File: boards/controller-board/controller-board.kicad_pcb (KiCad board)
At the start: 2 copper layers, 130 x 115 mm, 172 parts, among them J1 Conn_01x02, J2 Conn_01x02, J3 Conn_01x02, J4 Conn_01x02, J5 Conn_01x03, J6 Conn_01x02, Q1 Goford_G11S_20V_11A, Q2 PMV45EN, SW1 EG1271, U1 CAT4201, U10 CAT4201, U11 CAT4201, U12 CAT4201, U13 CAT4201, U14 CAT4201, U15 CAT4201, U17 CAT4201, U18 CAT4201, U25 RPi_Pico, U3 LTC3624, U4 CAT4201, U5 CAT4201, U6 CAT4201, U7 MCP4728, U8 ADS1015IRUGR, U9 ADS1015IRUGR

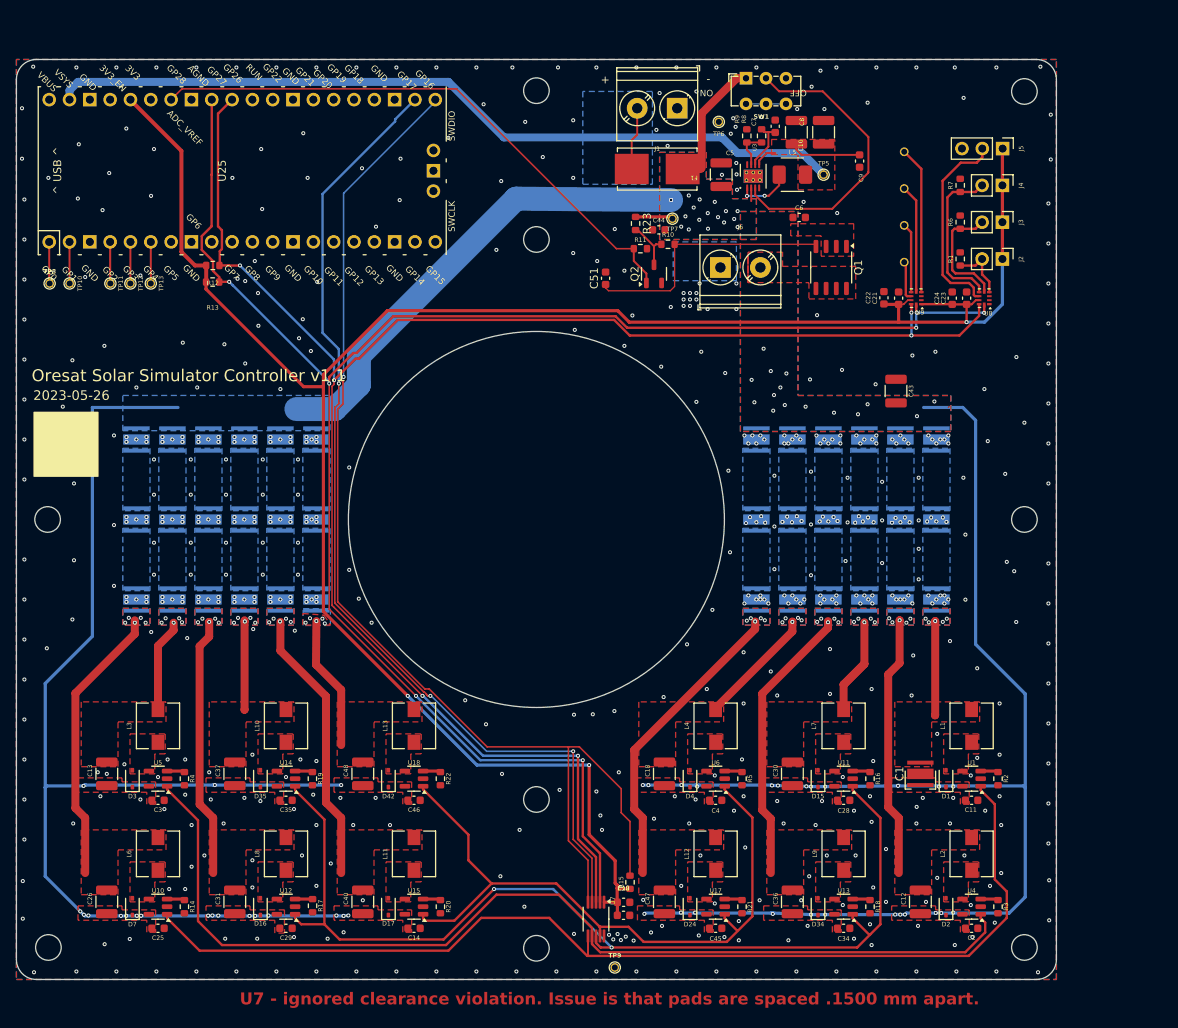
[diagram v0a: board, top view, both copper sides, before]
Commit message: added ground vias and changed ground pad filling on some components
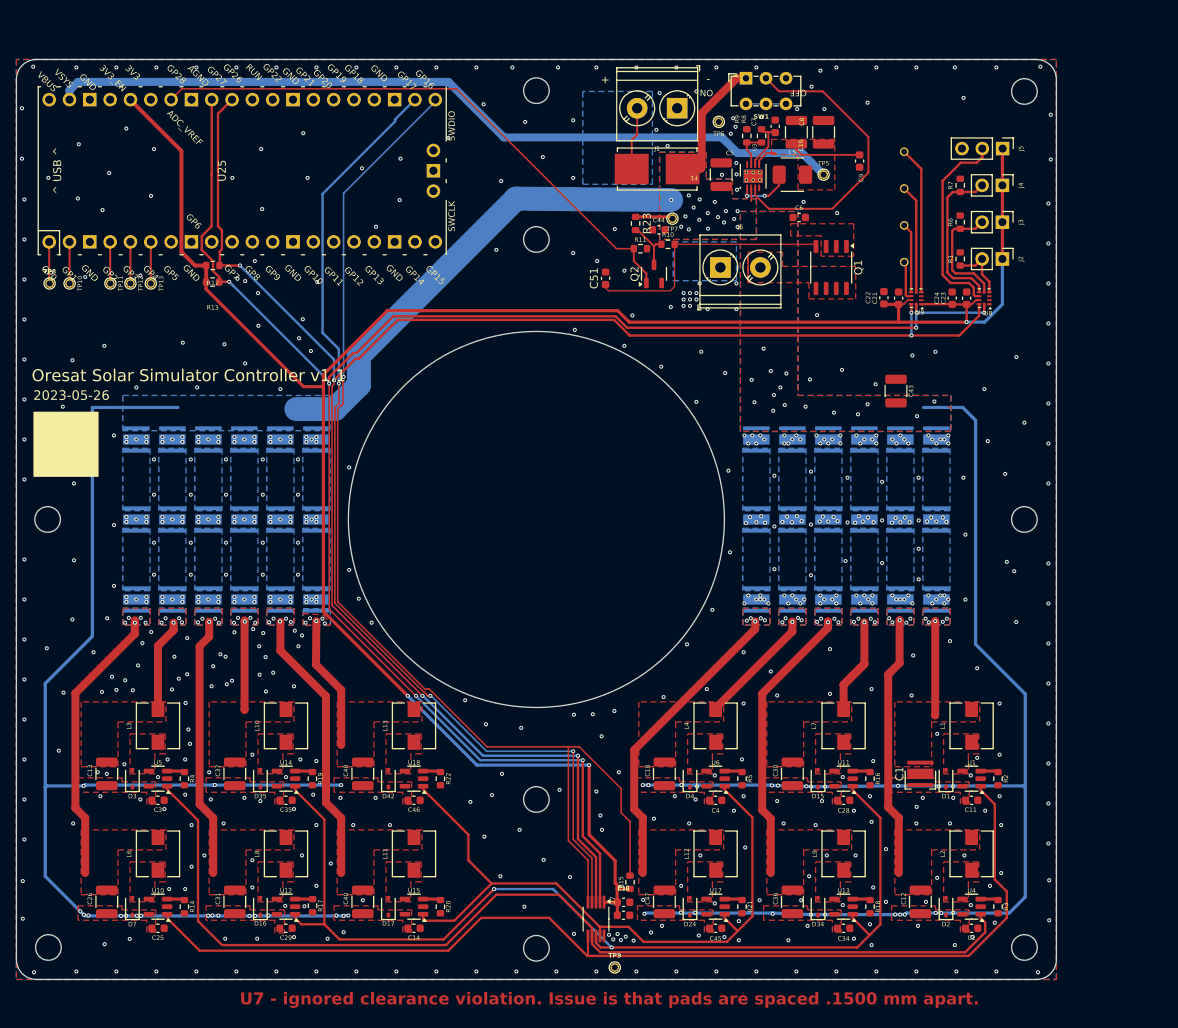
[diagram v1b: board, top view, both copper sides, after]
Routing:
- net VCC: vias 76 -> 75
- net GND: vias 591 -> 634

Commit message: added new design for LED driver portion of circuit with A6214
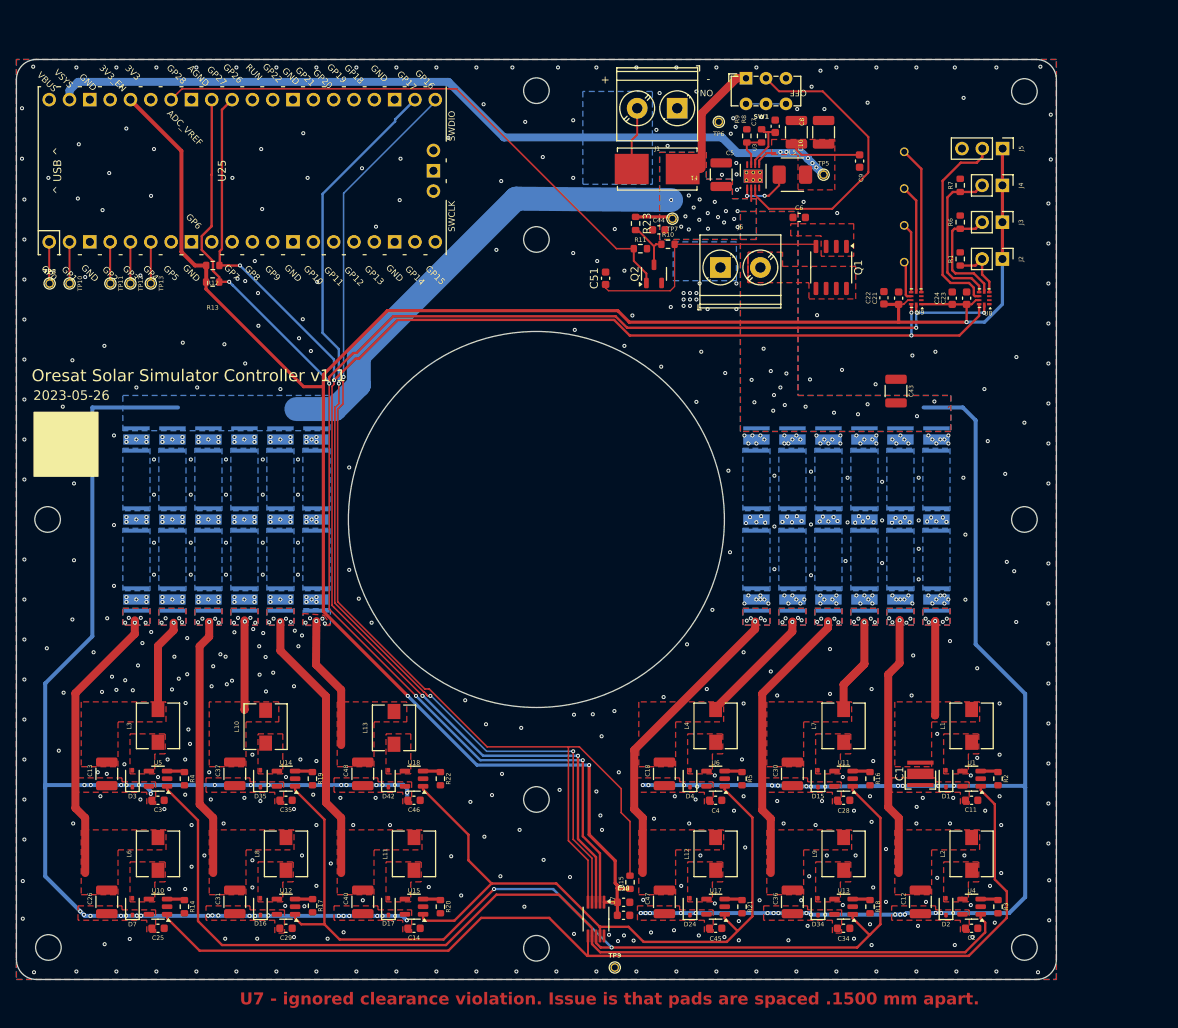
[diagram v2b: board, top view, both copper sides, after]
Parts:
- moved L10 2.55 mm to (111.2, 128.4)
- moved L13 2.51 mm to (127.2, 128.6)
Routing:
- net VCC: track 398.8 -> 417.2 mm, vias 75 -> 97
- net +5V: track 112.5 -> 111.9 mm, vias 0 -> 5
- net GND: vias 634 -> 635

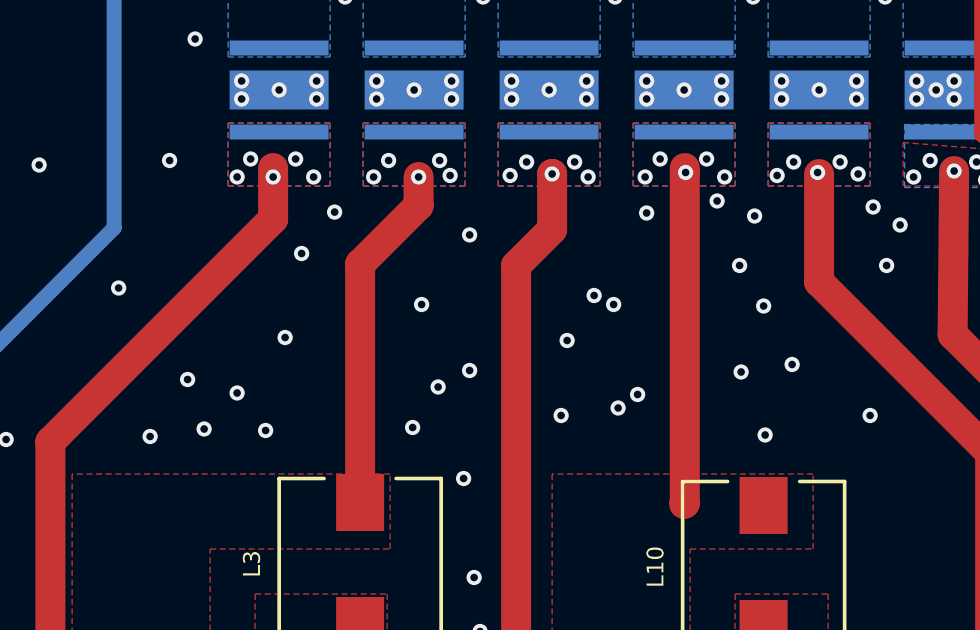
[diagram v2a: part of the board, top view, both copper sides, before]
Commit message: added project for test board for new LED driver
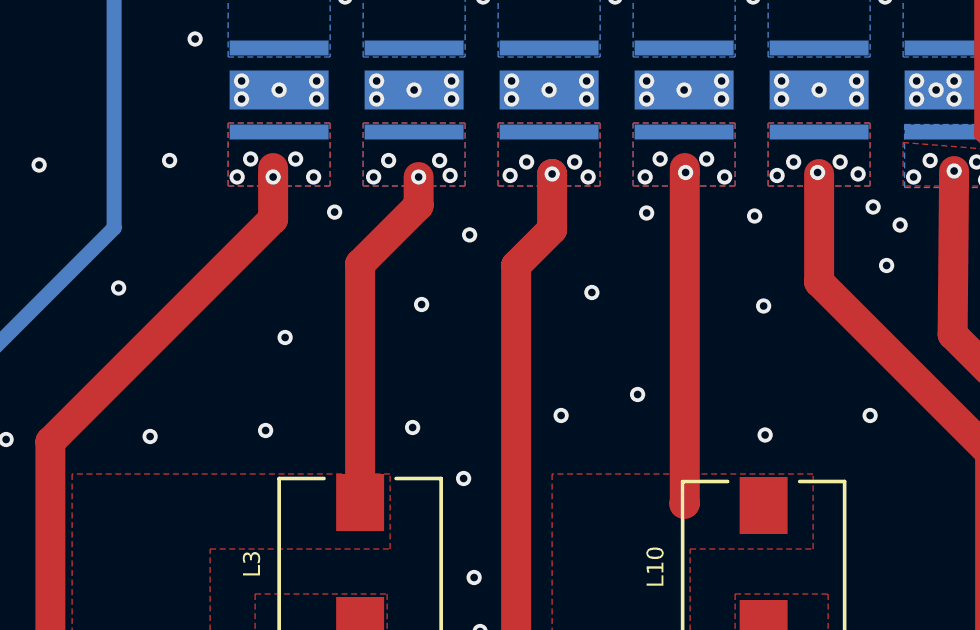
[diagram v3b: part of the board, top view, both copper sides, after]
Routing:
- net GND: vias 635 -> 622
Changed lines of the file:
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@@
 	)
 	(via
-		(at 110.4 121.9)
-		(size 0.508)
-		(drill 0.254)
-		(layers "F.Cu" "B.Cu")
-		(free yes)
-		(net 2)
-	)
-	(via
 		(at 180.4 102.75)
 		(size 0.508)
@@
 	)
 	(via
-		(at 112.1 121.65)
-		(size 0.508)
-		(drill 0.254)
-		(layers "F.Cu" "B.Cu")
-		(free yes)
-		(net 2)
-	)
-	(via
 		(at 198.628 104.394)
 		(size 0.508)
@@
 	)
 	(via
-		(at 110.35 118.35)
-		(size 0.508)
-		(drill 0.254)
-		(layers "F.Cu" "B.Cu")
-		(free yes)
-		(net 2)
-	)
-	(via
 		(at 162.3 137.1)
 		(size 0.508)
@@
 	)
 	(via
-		(at 92.5 123.8)
-		(size 0.508)
-		(drill 0.254)
-		(layers "F.Cu" "B.Cu")
-		(free yes)
-		(net 2)
-	)
-	(via
 		(at 117.5 132.7)
 		(size 0.508)
@@
 	)
 	(via
-		(at 93.6 122.6)
-		(size 0.508)
-		(drill 0.254)
-		(layers "F.Cu" "B.Cu")
-		(free yes)
-		(net 2)
-	)
-	(via
 		(at 96.83 62.05)
 		(size 0.508)
@@
 	)
 	(via
-		(at 104.6 120.85)
+		(at 105.425 119.25)
 		(size 0.508)
 		(drill 0.254)
@@
 	)
 	(via
-		(at 105.5 119.35)
-		(size 0.508)
-		(drill 0.254)
-		(layers "F.Cu" "B.Cu")
-		(free yes)
-		(net 2)
-	)
-	(via
 		(at 192.7 153.3)
 		(size 0.508)
@@
 	)
 	(via
-		(at 95.75 117.95)
-		(size 0.508)
-		(drill 0.254)
-		(layers "F.Cu" "B.Cu")
-		(free yes)
-		(net 2)
-	)
-	(via
 		(at 175.75 102.8)
 		(size 0.508)
@@
 	)
 	(via
-		(at 91.95 122.15)
-		(size 0.508)
-		(drill 0.254)
-		(layers "F.Cu" "B.Cu")
-		(free yes)
-		(net 2)
-	)
-	(via
 		(at 81 87.5)
 		(size 0.508)
@@
 	)
 	(via
-		(at 101.35 121.85)
-		(size 0.508)
-		(drill 0.254)
-		(layers "F.Cu" "B.Cu")
-		(free yes)
-		(net 2)
-	)
-	(via
 		(at 185.3 102.1)
 		(size 0.508)
@@
 	)
 	(via
-		(at 100.3 122.4)
-		(size 0.508)
-		(drill 0.254)
-		(layers "F.Cu" "B.Cu")
-		(free yes)
-		(net 2)
-	)
-	(via
 		(at 176.35 102.15)
 		(size 0.508)
@@
 	)
 	(via
-		(at 106.3 123.1)
-		(size 0.508)
-		(drill 0.254)
-		(layers "F.Cu" "B.Cu")
-		(free yes)
-		(net 2)
-	)
-	(via
 		(at 208 45.9)
 		(size 0.508)
@@
 	)
 	(via
-		(at 106.15 119.65)
-		(size 0.508)
-		(drill 0.254)
-		(layers "F.Cu" "B.Cu")
-		(free yes)
-		(net 2)
-	)
-	(via
 		(at 172.5 159)
 		(size 0.508)
@@
 	)
 	(via
-		(at 109.6 116.2)
-		(size 0.508)
-		(drill 0.254)
-		(layers "F.Cu" "B.Cu")
-		(free yes)
-		(net 2)
-	)
-	(via
 		(at 161.4 55.8)
 		(size 0.508)
@@
 		(polygon
 			(pts
-				(xy 113.3 134.3) (xy 110.2 134.3) (xy 110.2 129.3) (xy 113.3 129.3) (xy 113.3 131.8) (xy 113.3 131.8)
+				(xy 113.3 134.3) (xy 110.2 134.3) (xy 110.2 129.3) (xy 113.3 129.3) (xy 113.3 131.8)
 			)
 		)
@@
 		(polygon
 			(pts
-				(xy 129.3 134.3) (xy 126.2 134.3) (xy 126.2 129.3) (xy 129.3 129.3) (xy 129.3 131.8) (xy 129.3 131.8)
+				(xy 129.3 134.3) (xy 126.2 134.3) (xy 126.2 129.3) (xy 129.3 129.3) (xy 129.3 131.8)
 			)
 		)
